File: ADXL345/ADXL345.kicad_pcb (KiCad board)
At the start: 2 copper layers, 25.4 x 17.8 mm, 27 parts, among them J1 Conn_01x06, J2 Conn_01x04, J3 Conn_01x06, J4 Conn_01x04, Q1 BSS138DW, Q2 BSS138DW, U1 AP2127K-3.3, U2 ADXL345

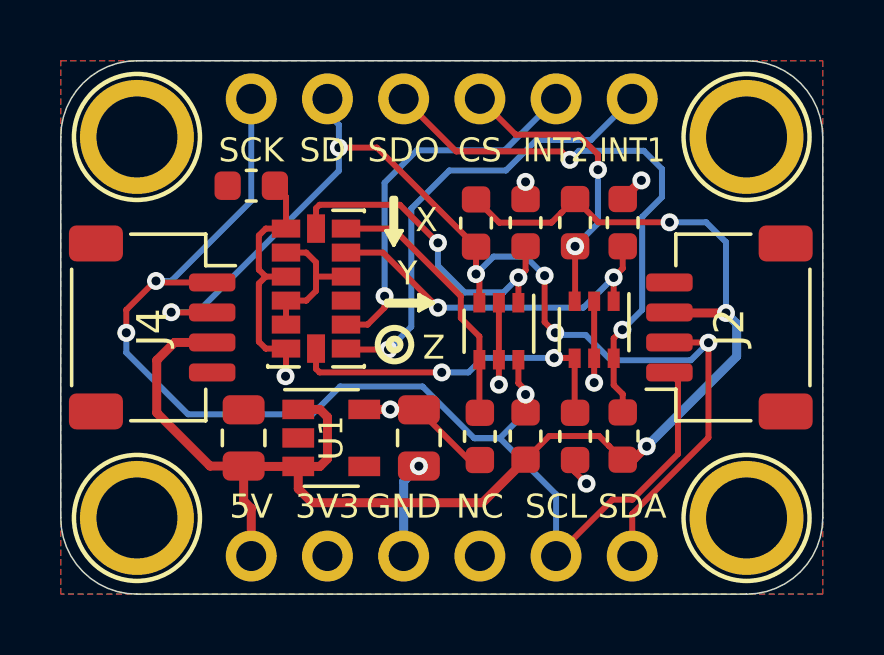
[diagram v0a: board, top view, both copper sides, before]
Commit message: Copper Pour Edits
Copper pour reduced to have 0.2mm edge clearance
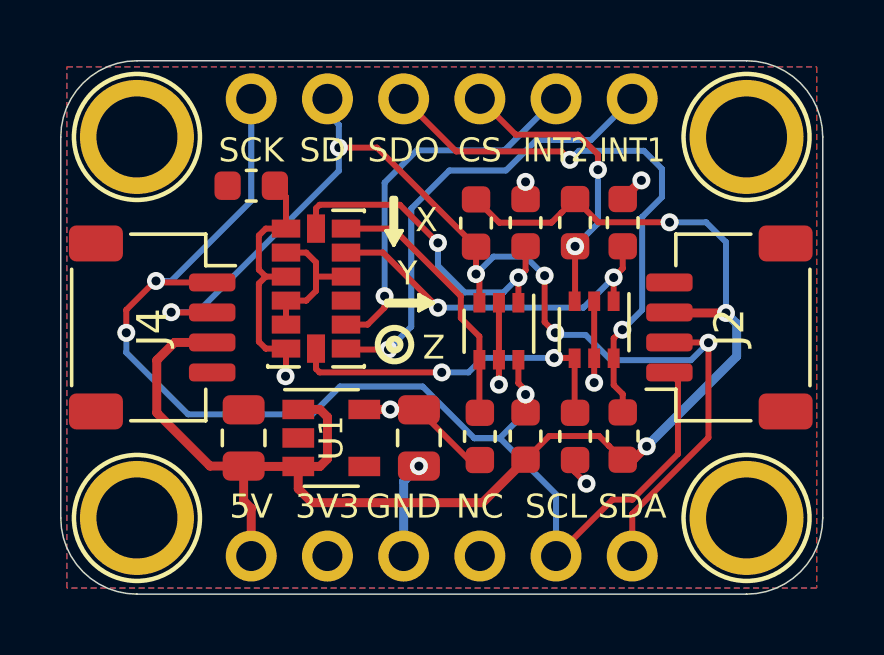
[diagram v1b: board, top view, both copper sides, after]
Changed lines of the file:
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@@
     (polygon
       (pts
-        (xy 52.578 27.0764) (xy 77.978 27.0764) (xy 77.978 44.8564) (xy 52.578 44.8564)
+        (xy 52.7812 27.2796) (xy 77.7748 27.2796) (xy 77.7748 44.6532) (xy 52.7812 44.6532)
       )
     )
@@
     (polygon
       (pts
-        (xy 52.578 27.0764) (xy 77.978 27.0764) (xy 77.978 44.8564) (xy 52.578 44.8564)
+        (xy 52.7812 27.2796) (xy 77.7748 27.2796) (xy 77.7748 44.6532) (xy 52.7812 44.6532)
       )
     )

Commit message: ADXL345 Silkscreen edit
ADXL345 Added to front silkscreen
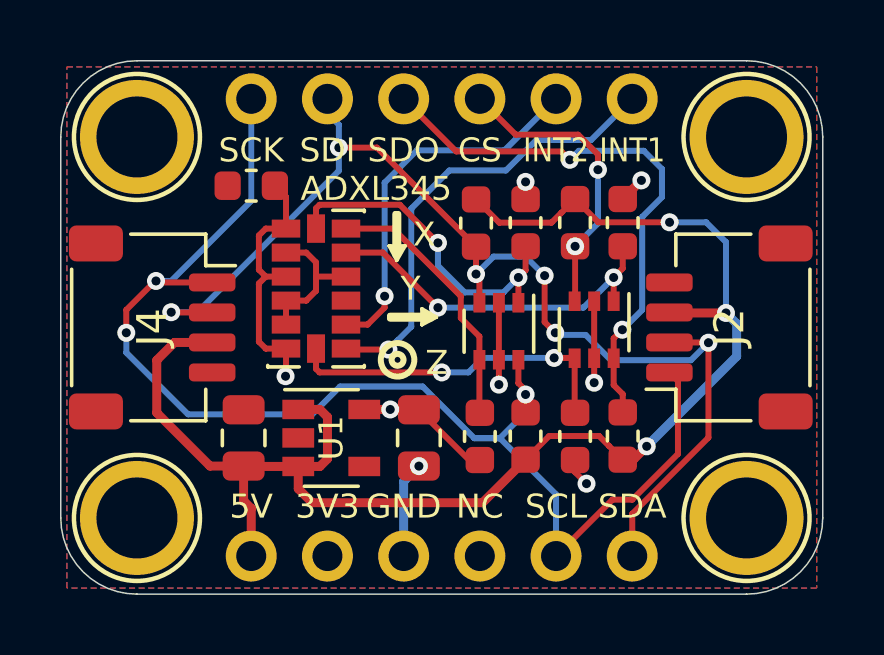
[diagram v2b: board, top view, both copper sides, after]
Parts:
- renumbered U2 to ADXL345
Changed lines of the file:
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@@
   )
   (layers
-    (0 F.Cu signal)
-    (31 B.Cu signal)
+    (0 F.Cu signal hide)
+    (31 B.Cu signal hide)
     (32 B.Adhes user hide)
     (33 F.Adhes user hide)
@@
     (35 F.Paste user hide)
     (36 B.SilkS user)
-    (37 F.SilkS user)
-    (38 B.Mask user hide)
+    (37 F.SilkS user hide)
+    (38 B.Mask user)
     (39 F.Mask user hide)
     (40 Dwgs.User user)
@@
     (tags "LGA LGA")
     (attr smd)
-    (fp_text reference U2 (at 0 0 90) (layer F.SilkS) hide
-      (effects (font (size 1 1) (thickness 0.15)))
+    (fp_text reference ADXL345 (at 2.0066 -3.3274 180) (layer F.SilkS)
+      (effects (font (size 0.8 0.8) (thickness 0.12)))
     )
     (fp_text value ADXL345 (at 0 3.45) (layer F.Fab)
@@
     )
   )
-  (gr_line (start 64.9986 35.1536) (end 64.516 35.4076) (layer F.SilkS) (width 0.12))
-  (gr_line (start 64.9986 35.1536) (end 64.516 34.8742) (layer F.SilkS) (width 0.12))
-  (gr_line (start 63.4492 35.2044) (end 64.8208 35.2044) (layer F.SilkS) (width 0.2))
-  (gr_line (start 63.4492 35.1028) (end 64.8208 35.1028) (layer F.SilkS) (width 0.2))
-  (gr_line (start 63.4492 35.1536) (end 64.8208 35.1536) (layer F.SilkS) (width 0.2))
-  (gr_line (start 64.516 34.8742) (end 64.516 35.4076) (layer F.SilkS) (width 0.12))
-  (gr_line (start 64.5922 34.9504) (end 64.5922 35.3314) (layer F.SilkS) (width 0.12))
-  (gr_line (start 63.881 32.8168) (end 63.5 32.8168) (layer F.SilkS) (width 0.12))
-  (gr_line (start 63.9572 32.7406) (end 63.4238 32.7406) (layer F.SilkS) (width 0.12))
-  (gr_line (start 63.6778 31.6738) (end 63.6778 33.0454) (layer F.SilkS) (width 0.2))
-  (gr_line (start 63.7286 31.6738) (end 63.7286 33.0454) (layer F.SilkS) (width 0.2))
-  (gr_line (start 63.627 31.6738) (end 63.627 33.0454) (layer F.SilkS) (width 0.2))
-  (gr_line (start 63.6778 33.2232) (end 63.9572 32.7406) (layer F.SilkS) (width 0.12))
-  (gr_line (start 63.6778 33.2232) (end 63.4238 32.7406) (layer F.SilkS) (width 0.12))
-  (gr_circle (center 63.7032 36.5379) (end 64.262 36.5379) (layer F.SilkS) (width 0.2))
-  (gr_circle (center 63.7032 36.5379) (end 63.8032 36.5379) (layer F.SilkS) (width 0.4))
-  (gr_text X (at 64.77 32.385) (layer F.SilkS)
+  (gr_line (start 65.1002 35.6235) (end 64.6176 35.8775) (layer F.SilkS) (width 0.12))
+  (gr_line (start 65.1002 35.6235) (end 64.6176 35.3441) (layer F.SilkS) (width 0.12))
+  (gr_line (start 63.5508 35.6743) (end 64.9224 35.6743) (layer F.SilkS) (width 0.2))
+  (gr_line (start 63.5508 35.5727) (end 64.9224 35.5727) (layer F.SilkS) (width 0.2))
+  (gr_line (start 63.5508 35.6235) (end 64.9224 35.6235) (layer F.SilkS) (width 0.2))
+  (gr_line (start 64.6176 35.3441) (end 64.6176 35.8775) (layer F.SilkS) (width 0.12))
+  (gr_line (start 64.6938 35.4203) (end 64.6938 35.8013) (layer F.SilkS) (width 0.12))
+  (gr_line (start 63.9826 33.3248) (end 63.6016 33.3248) (layer F.SilkS) (width 0.12))
+  (gr_line (start 64.0588 33.2486) (end 63.5254 33.2486) (layer F.SilkS) (width 0.12))
+  (gr_line (start 63.7794 32.1818) (end 63.7794 33.5534) (layer F.SilkS) (width 0.2))
+  (gr_line (start 63.8302 32.1818) (end 63.8302 33.5534) (layer F.SilkS) (width 0.2))
+  (gr_line (start 63.7286 32.1818) (end 63.7286 33.5534) (layer F.SilkS) (width 0.2))
+  (gr_line (start 63.7794 33.7312) (end 64.0588 33.2486) (layer F.SilkS) (width 0.12))
+  (gr_line (start 63.7794 33.7312) (end 63.5254 33.2486) (layer F.SilkS) (width 0.12))
+  (gr_circle (center 63.8048 37.0459) (end 64.3636 37.0459) (layer F.SilkS) (width 0.2))
+  (gr_circle (center 63.8048 37.0459) (end 63.9048 37.0459) (layer F.SilkS) (width 0.4))
+  (gr_text X (at 64.6938 32.8676) (layer F.SilkS)
     (effects (font (size 0.8 0.8) (thickness 0.13)))
   )
-  (gr_text Z (at 65.0113 36.576 180) (layer F.SilkS)
+  (gr_text Z (at 65.1129 37.084 180) (layer F.SilkS)
     (effects (font (size 0.8 0.8) (thickness 0.13)))
   )
-  (gr_text Y (at 64.135 34.163) (layer F.SilkS)
+  (gr_text Y (at 64.2366 34.671) (layer F.SilkS)
     (effects (font (size 0.8 0.8) (thickness 0.13)))
   )

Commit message: Soldermask width adjusted
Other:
- rule solder_mask_min_width: 0.1 -> 0.05
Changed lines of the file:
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@@
   )
   (layers
-    (0 F.Cu signal hide)
-    (31 B.Cu signal hide)
+    (0 F.Cu signal)
+    (31 B.Cu signal)
     (32 B.Adhes user hide)
     (33 F.Adhes user hide)
@@
     (35 F.Paste user hide)
     (36 B.SilkS user)
-    (37 F.SilkS user hide)
-    (38 B.Mask user)
+    (37 F.SilkS user)
+    (38 B.Mask user hide)
     (39 F.Mask user hide)
     (40 Dwgs.User user)
@@
     (pad_drill 1)
     (pad_to_mask_clearance 0)
-    (solder_mask_min_width 0.1)
+    (solder_mask_min_width 0.05)
     (aux_axis_origin 0 0)
     (visible_elements 7FFFFFFF)
